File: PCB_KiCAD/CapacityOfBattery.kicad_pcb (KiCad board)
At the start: 2 copper layers, 31.1 x 57.6 mm, 35 parts, among them J1 BATTERY, J2 DUT, Q1 IRLML6401TRPBF, Q2 IRLML6401TRPBF, Q3 IRLML6401TRPBF, Q4 IRLML6401TRPBF, Q5 SI2302, SW1 SW_Push

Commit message: updated BOM
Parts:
- renumbered REF** to ?
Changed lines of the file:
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@@
       (padsonsilk false)
       (subtractmaskfromsilk false)
-      (outputformat 4)
+      (outputformat 1)
       (mirror false)
       (drillshape 0)
@@
     (tags "Logo Symbol OSHW")
     (attr virtual)
-    (fp_text reference REF** (at 0 0) (layer F.SilkS) hide
-      (effects (font (size 1 1) (thickness 0.15)))
-    )
+    (fp_text reference "" (at 0 0) (layer F.SilkS) hide
+      (effects (font (size 1 1) (thickness 0.15)))
+    )

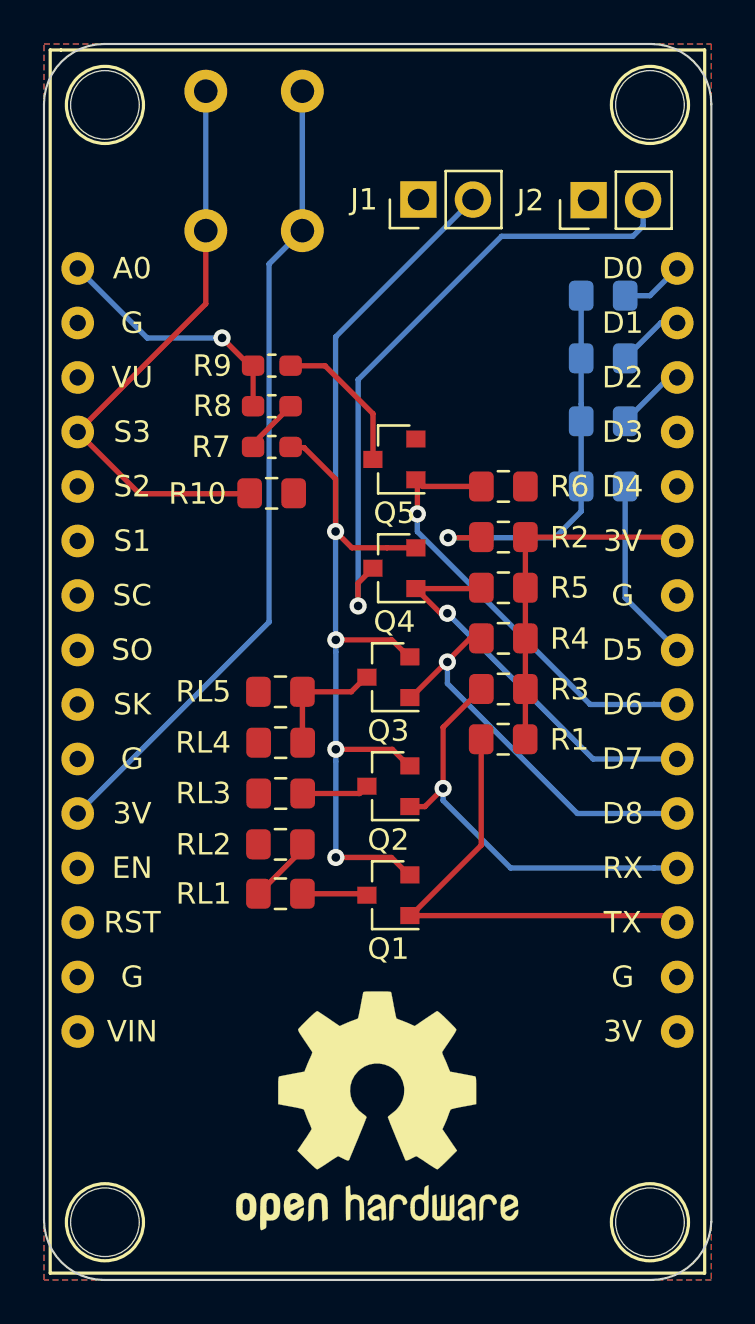
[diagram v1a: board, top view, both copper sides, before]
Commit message: changed folders and libraries
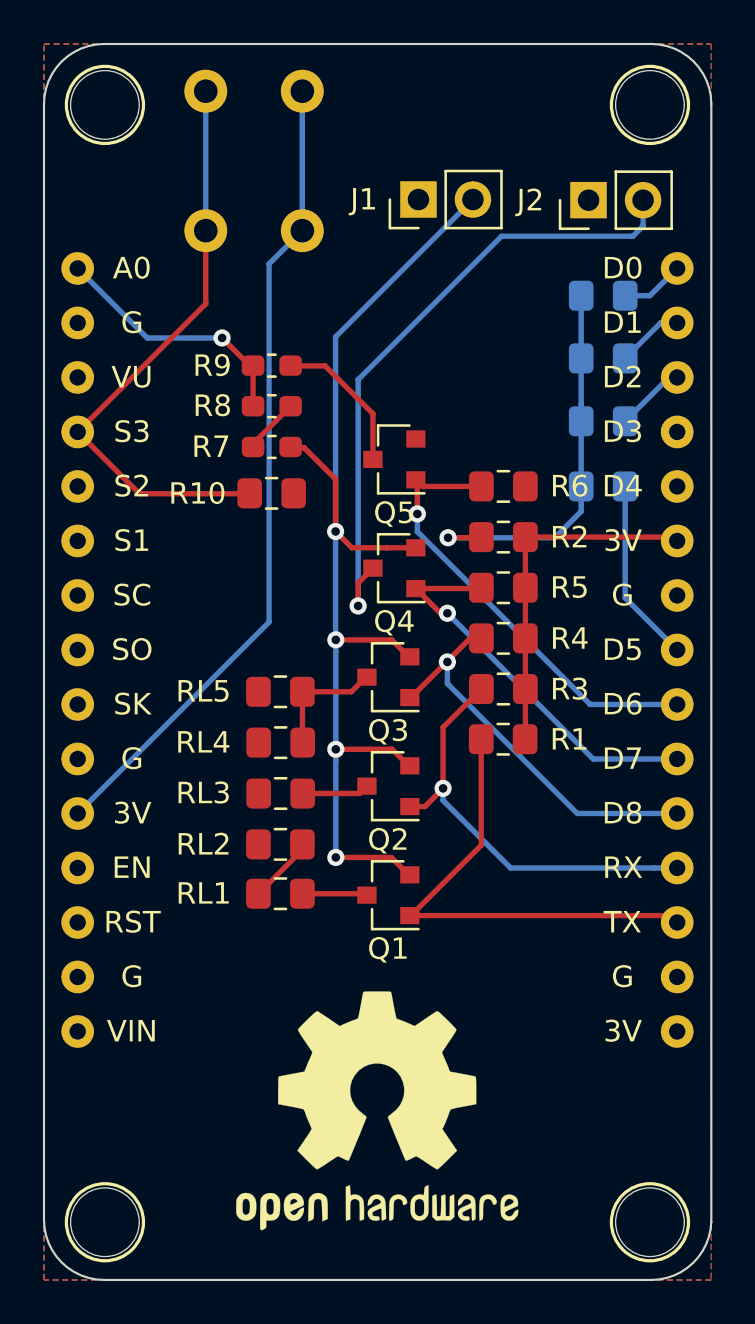
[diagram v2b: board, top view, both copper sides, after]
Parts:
- ?: footprint SUDHEENDRA_HEGDE:NodeMCU-LoLinV3 -> lib_KiCAD:NodeMCU-LoLinV3_without_border
- D1, D2, D3, D4: footprint LED_SMD:LED_0805_2012Metric_Pad1.15x1.40mm_HandSolder -> lib_fp:LED_0805_2012Metric_Pad1.15x1.40mm_HandSolder
- J1, J2: footprint Connector_PinHeader_2.54mm:PinHeader_1x02_P2.54mm_Vertical -> lib_fp:PinHeader_1x02_P2.54mm_Vertical
- Q1, Q2, Q3, Q4: footprint Package_TO_SOT_SMD:SOT-23 -> lib_fp:SOT-23
- R1, R10, R2, R3, R4, R5, R6, RL1, RL2, RL3, RL4, RL5: footprint Resistor_SMD:R_0805_2012Metric_Pad1.15x1.40mm_HandSolder -> lib_fp:R_0805_2012Metric_Pad1.15x1.40mm_HandSolder
- R7, R8, R9: footprint Resistor_SMD:R_0603_1608Metric_Pad1.05x0.95mm_HandSolder -> lib_fp:R_0603_1608Metric_Pad1.05x0.95mm_HandSolder
- SW1: footprint Button_Switch_THT:SW_PUSH_6mm -> lib_fp:SW_PUSH_6mm

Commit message: modified position of J2
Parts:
- removed the ? at (28.8, 62.1)
- added ?: OSHW-Logo2_9.8x8mm_SilkScreen, Symbol:OSHW-Logo2_9.8x8mm_SilkScreen, F.Cu at (24.9, 63.6)
- moved J2 43.3 mm to (35.8, 62.9), turned to 270 degrees
- moved ? 5.51 mm to (30.1, 55.5)
- moved J1 2.52 mm to (33.3, 19.6)
- moved ? 1.08 mm to (28.7, 41.8)
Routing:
- net /dut: track 30.0 -> 28.7 mm
- net /Vbat: track 53.8 -> 54.9 mm
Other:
- board text added: "appiko.org"
